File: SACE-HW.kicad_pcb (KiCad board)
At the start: 2 copper layers, 100 x 100 mm, 189 parts, among them IC201 1769205241, J201 Header_Male_Pin_2.54mm_1X2_,_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, J202 1935161, J203 2350514-8, J301 Header_Male_Pin_2.54mm_1X6_,_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, J302 XH-4A connector, J401 1935161, J402 1935161, J403 RF1-01K-D-00-50-BK-HDW, J404 RF1-01K-D-00-50-BK-HDW, J501 Header_Male_Pin_2.54mm_1X4_,_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, J502 690-005-299-043, J601 XH-4A connector, J602 XH-4A connector, J603 2350514-8, J604 2350514-8, J605 2350514-8, J701 2350514-8, J801 MEM2075-00-140-01-A, J901 2350514-8, J902 2350514-8, Q401 MCB90N12A-TP, Q901 PMV20XNER, Q902 PMV20XNER, Q903 PMV20XNER, Q904 PMV20XNER, Q905 PMV20XNER, Q906 PMV20XNER, Q907 PMV20XNER, Q908 PMV20XNER, SW301 PTS645SM43SMTR92, SW302 PTS645SM43SMTR92, U201 AZ1117IH-3.3TRG1, U202 OKI-78SR-5_1.5-W36H-C, U203 AZ1117IH-3.3TRG1, U301 STM32F446RE, U401 LTV-816S, U402 TMCS1101A3UQDT, U403 MCP6L04T-E/SL, U501 MCP2221A-I_SL, U601 MCP4728T-E_UN, U602 TLA2528IRTER, U603 TLV9302IDR, U604 TLA2528IRTER, U701 74LVC4245APW_118

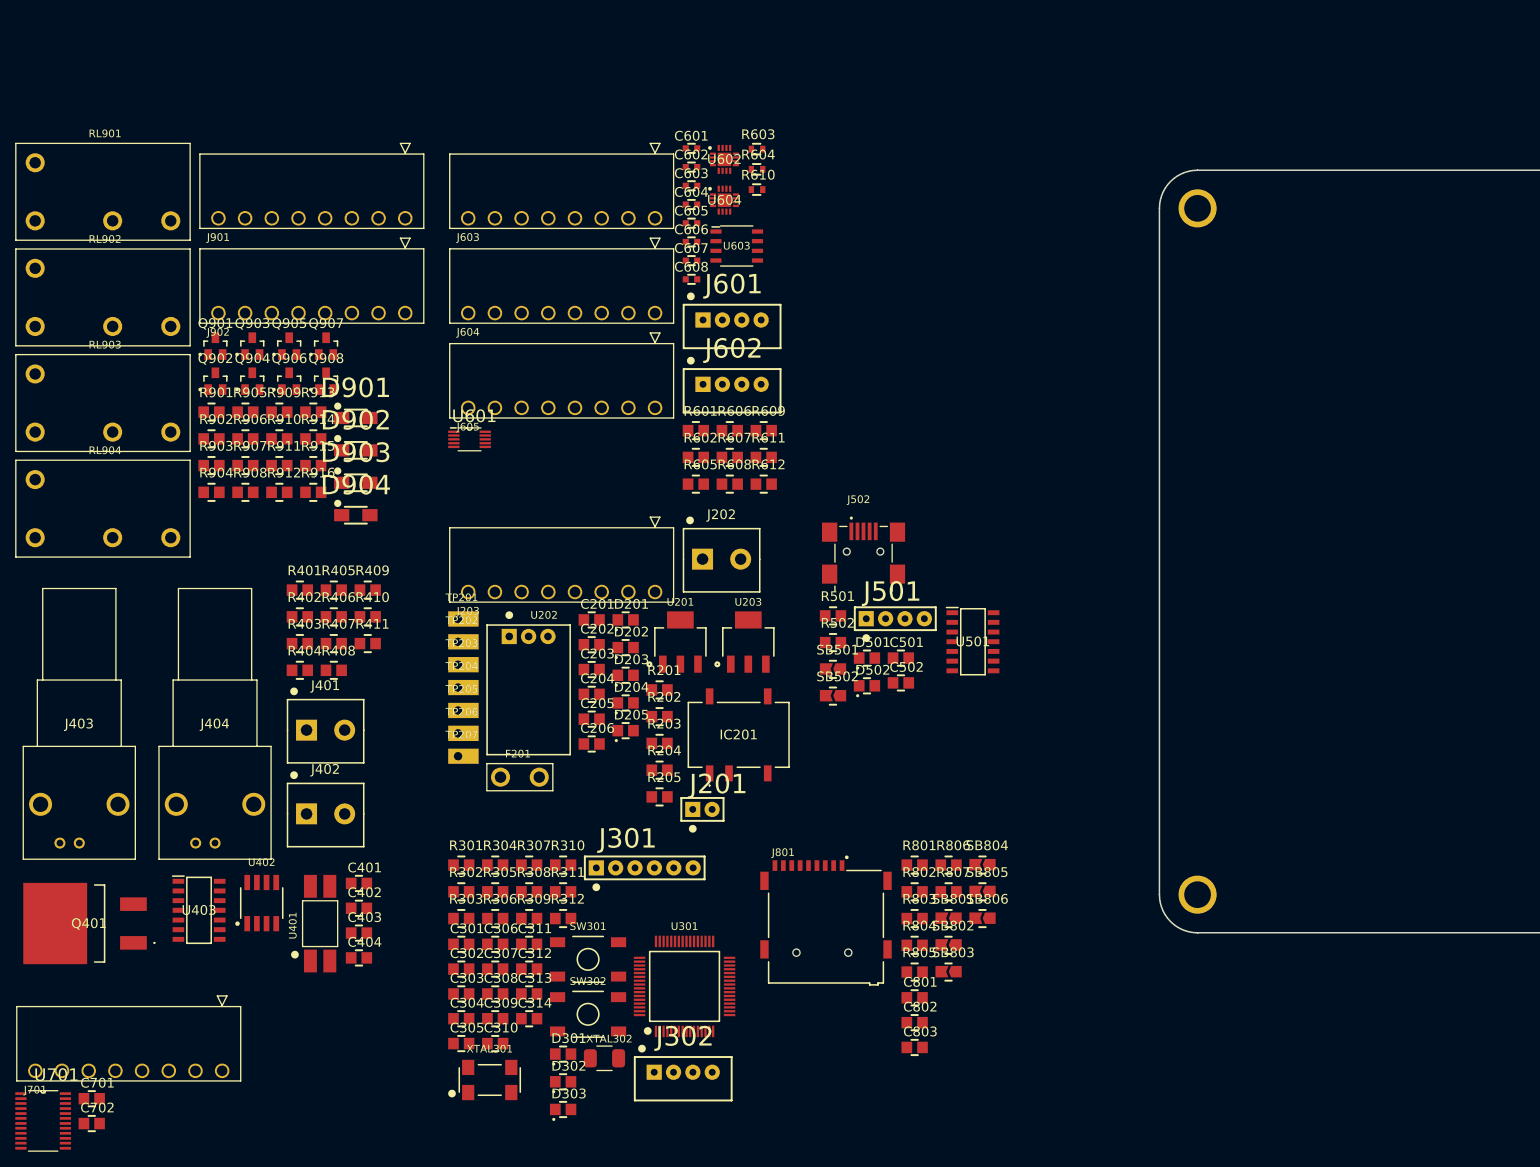
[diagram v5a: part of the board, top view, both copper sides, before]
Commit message: update schematic
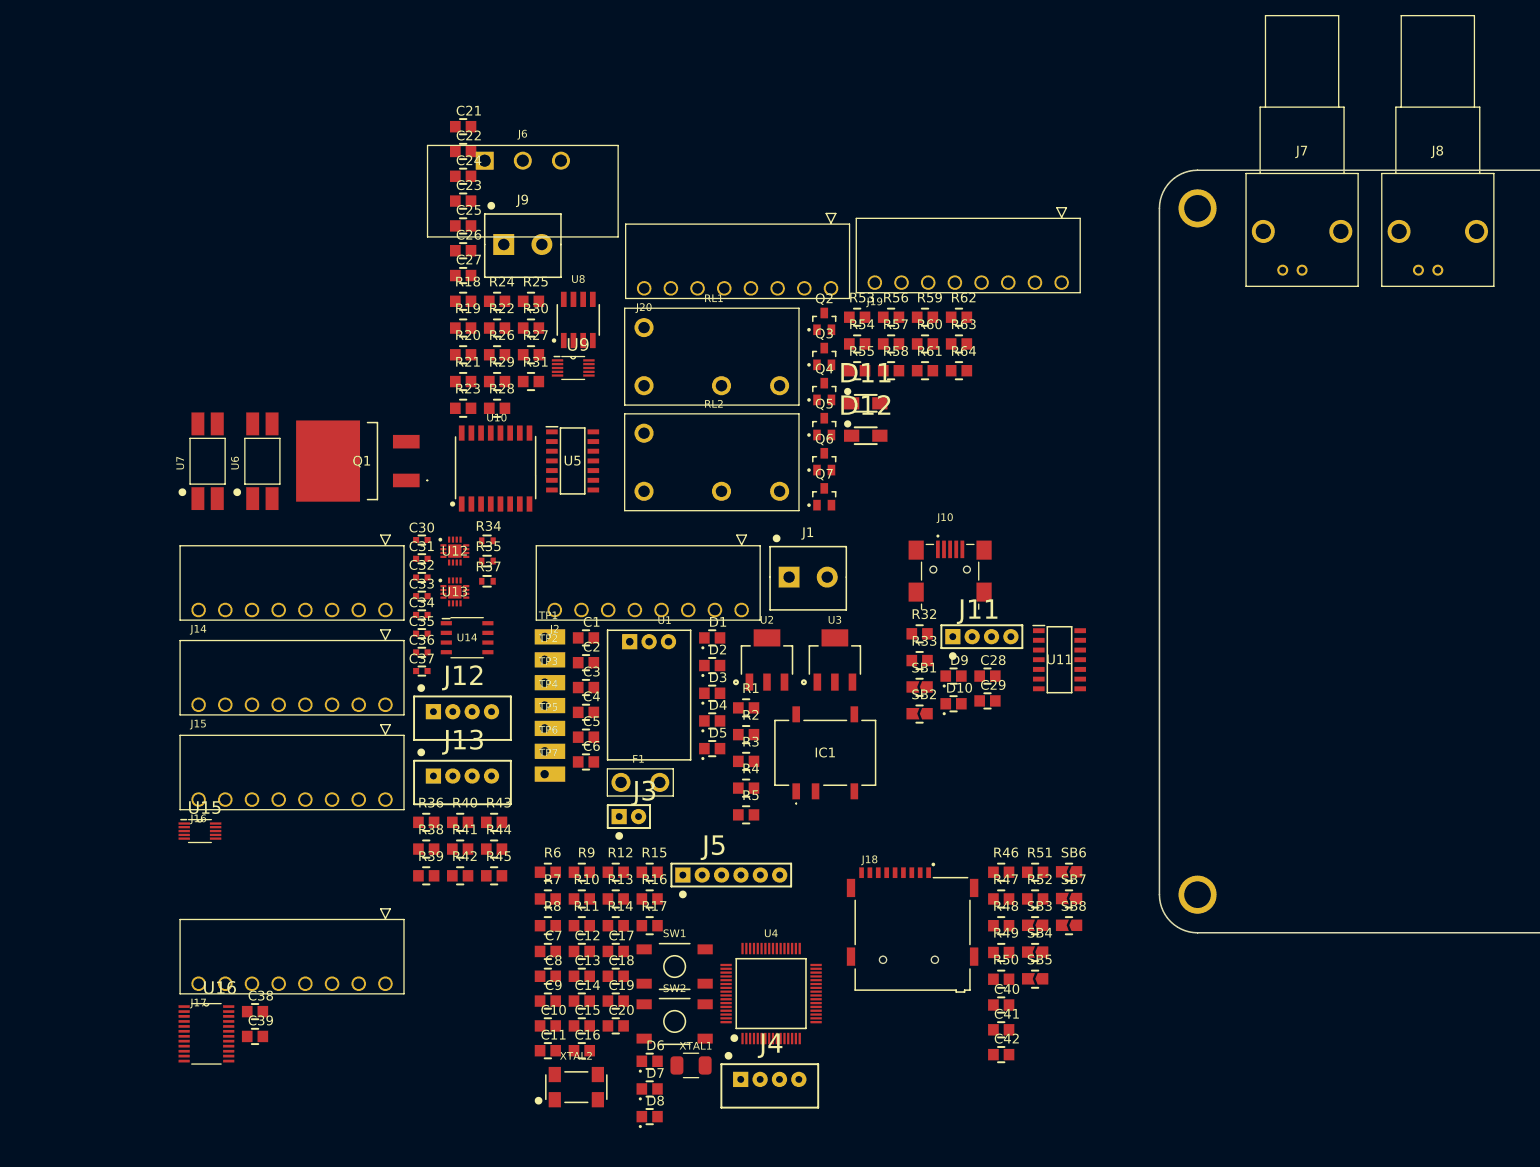
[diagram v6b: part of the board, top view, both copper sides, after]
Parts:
- removed C201, C203: 885012107005, Capacitors:C0805
- removed C202, C206: 885012107014, Capacitors:C0805
- removed C204, C205, C312: 885012107018, Capacitors:C0805
- removed C301, C307, C310, C311, C313, C314, C401, C403, C501, C502, C701, C702, C802, C803: 885012207098, Capacitors:C0805
- removed C302, C303: 885012007027, Capacitors:C0805
- removed C304, C308, C801: 885012107015, Capacitors:C0805
- removed C305, C306: 885012007053, Capacitors:C0805
- removed C309: 885012207092, Capacitors:C0805
- removed C402, C404: 885012207103, Capacitors:C0805
- removed C601, C602, C603, C604, C605, C606, C607, C608: 885012107015, Capacitors:C0603
- removed D201, D202, D203, D204, D205, D301, D501: 150080VS75000, Diodes:LED_0805_GREEN
- removed D302, D502: 150080YS75000, Diodes:LED_0805_YELLOW
- removed D303: 150080RS75000, Diodes:LED_0805_RED
- removed D901, D902, D903, D904: DSS16U, Diodes:SOD-123FL
- removed F201: 39511000440, Fuses:TE5_395
- removed IC201: 1769205241, IC:1769205241
- removed J201: Header_Male_Pin_2.54mm_1X2_,_Unshrouded, Connectors:Headers_2.54mm_1X2
- removed J202, J401, J402: 1935161, Connectors:1935161
- removed J203, J603, J604, J605, J701, J901, J902: 2350514-8, Connectors:CONN8_2350514-8_TEC
- removed J301: Header_Male_Pin_2.54mm_1X6_,_Unshrouded, Connectors:Headers_2.54mm_1X6
- removed J302, J601, J602: XH-4A connector, Connectors:XH-4A
- removed J403, J404: RF1-01K-D-00-50-BK-HDW, Connectors:RF101KD0050
- removed J501: Header_Male_Pin_2.54mm_1X4_,_Unshrouded, Connectors:Headers_2.54mm_1X4
- removed J502: 690-005-299-043, Connectors:EDAC_690-005-299-043
- removed J801: MEM2075-00-140-01-A, Connectors:GCT_MEM2075-00-140-01-A
- removed Q401: MCB90N12A-TP, IC:MCB90N12ATP
- removed Q901, Q902, Q903, Q904, Q905, Q906, Q907, Q908: PMV20XNER, IC:SOT-23-3
- removed R201, R204, R403, R405, R406, R408, R410: RC0805FR-075K6L, Resistors:R0805
- removed R202, R205, R310, R311, R312, R402, R501, R502, R605, R609: RC0805JR-072K2L, Resistors:R0805
- removed R203: RC0805JR-0733KL, Resistors:R0805
- removed R301, R606, R607, R611, R612, R905, R906, R907, R908, R913, R914, R915, R916: RC0805JR-0710KL, Resistors:R0805
- removed R302, R303: RC0805JR-070RL, Resistors:R0805
- removed R304, R305, R601, R602: RC0805JR-074K7L, Resistors:R0805
- removed R306, R307, R802: RC0805JR-07150RL, Resistors:R0805
- removed R308, R309: RC0805JR-07470RL, Resistors:R0805
- removed R401, R901, R902, R903, R904, R909, R910, R911, R912: RC0805JR-07330RL, Resistors:R0805
- removed R404, R409: RMCF0805FT10M0, Resistors:R0805
- removed R407, R411: RC0805FR-07200KL, Resistors:R0805
- removed R603, R604, R610: RC0805JR-070RL, Resistors:R0603
- removed R608: RC0805JR-07100KL, Resistors:R0805
- removed R801, R803, R804, R805, R806, R807: RC0805FR-0747KL, Resistors:R0805
- removed RL901, RL902, RL903, RL904: ALQ312, Relays:ALQ312
- removed SB501, SB502, SB801, SB802, SB803, SB804, SB805, SB806: Solder_Bridge, Connectors:Solder_bridge_0805
- removed SW301, SW302: PTS645SM43SMTR92, Switches:PTS645_6X6X4_SMD
- removed TP201, TP202, TP203, TP204, TP205, TP206, TP207: Test_Point_THM, Connectors:Keystone_5001
- removed U201, U203: AZ1117IH-3.3TRG1, IC:SOT-223-3
- removed U202: OKI-78SR-5_1.5-W36H-C, Assembly:OKI-78SR_Horizontal
- removed U301: STM32F446RE, IC:LQFP-64
- removed U401: LTV-816S, IC:4-SMD
- removed U402: TMCS1101A3UQDT, IC:SOIC-8
- removed U403: MCP6L04T-E/SL, IC:SOIC127P600X175-14N
- removed U501: MCP2221A-I_SL, IC:SOIC127P600X175-14N
- removed U601: MCP4728T-E_UN, IC:SOP50P490X110-10N
- removed U602, U604: TLA2528IRTER, IC:QFN50P300X300X80-17N-D
- removed U603: TLV9302IDR, Assembly:IC8_TLV9302IDR_TEX
- removed U701: 74LVC4245APW_118, IC:SOP65P640X110-24N
- removed XTAL301: ABS25-32.768KHZ-6-T, Crystals:ABS25
- removed XTAL302: 7A-8.000MAHJ-T, Crystals:TXC_7A_Series
- added C1: 885012107018, Capacitors:C0805, F.Cu at (94.3, 85.1)
- added C10: 885012007027, Capacitors:C0805, F.Cu at (89.3, 136.0)
- added C11: 885012107015, Capacitors:C0805, F.Cu at (89.3, 139.3)
- added C12: 885012207092, Capacitors:C0805, F.Cu at (93.7, 126.2)
- added C13: 885012007027, Capacitors:C0805, F.Cu at (93.7, 129.5)
- added C14: 885012107015, Capacitors:C0805, F.Cu at (93.7, 132.8)
- added C15: 885012207098, Capacitors:C0805, F.Cu at (93.7, 136.0)
- added C16: 885012207098, Capacitors:C0805, F.Cu at (93.7, 139.3)
- added C17: 885012107018, Capacitors:C0805, F.Cu at (98.2, 126.2)
- added C18: 885012207098, Capacitors:C0805, F.Cu at (98.2, 129.5)
- added C19: 885012207098, Capacitors:C0805, F.Cu at (98.2, 132.8)
- added C2: 885012107018, Capacitors:C0805, F.Cu at (94.3, 88.4)
- added C20: 885012207098, Capacitors:C0805, F.Cu at (98.2, 136.0)
- added C21: 885012207103, Capacitors:C0805, F.Cu at (78.2, 18.1)
- added C22: 885012207098, Capacitors:C0805, F.Cu at (78.2, 21.3)
- added C23: 885012207098, Capacitors:C0805, F.Cu at (78.2, 27.8)
- added C24: 885012207103, Capacitors:C0805, F.Cu at (78.2, 24.6)
- added C25: 885012207103, Capacitors:C0805, F.Cu at (78.2, 31.1)
- added C26: 885012207098, Capacitors:C0805, F.Cu at (78.2, 34.4)
- added C27: 885012207103, Capacitors:C0805, F.Cu at (78.2, 37.6)
- added C28: 885012207098, Capacitors:C0805, F.Cu at (146.9, 90.1)
- added C29: 885012207098, Capacitors:C0805, F.Cu at (146.9, 93.4)
- added C3: 885012107014, Capacitors:C0805, F.Cu at (94.3, 91.6)
- added C30: 885012107015, Capacitors:C0603, F.Cu at (73.0, 72.3)
- added C31: 885012107015, Capacitors:C0603, F.Cu at (73.0, 74.8)
- added C32: 885012107015, Capacitors:C0603, F.Cu at (73.0, 77.2)
- added C33: 885012107015, Capacitors:C0603, F.Cu at (73.0, 79.7)
- added C34: 885012107015, Capacitors:C0603, F.Cu at (73.0, 82.1)
- added C35: 885012107015, Capacitors:C0603, F.Cu at (73.0, 84.6)
- added C36: 885012107015, Capacitors:C0603, F.Cu at (73.0, 87.0)
- added C37: 885012107015, Capacitors:C0603, F.Cu at (73.0, 89.5)
- added C38: 885012207098, Capacitors:C0805, F.Cu at (50.9, 134.1)
- added C39: 885012207098, Capacitors:C0805, F.Cu at (50.9, 137.4)
- added C4: 885012107014, Capacitors:C0805, F.Cu at (94.3, 94.9)
- added C40: 885012207098, Capacitors:C0805, F.Cu at (148.7, 133.3)
- added C41: 885012107015, Capacitors:C0805, F.Cu at (148.7, 136.5)
- added C42: 885012207098, Capacitors:C0805, F.Cu at (148.7, 139.8)
- added C5: 885012107005, Capacitors:C0805, F.Cu at (94.3, 98.1)
- added C6: 885012107005, Capacitors:C0805, F.Cu at (94.3, 101.4)
- added C7: 885012007053, Capacitors:C0805, F.Cu at (89.3, 126.2)
- added C8: 885012207098, Capacitors:C0805, F.Cu at (89.3, 129.5)
- added C9: 885012007053, Capacitors:C0805, F.Cu at (89.3, 132.8)
- added D1: 150080VS75000, Diodes:LED_0805_GREEN, F.Cu at (110.8, 85.1)
- added D10: 150080YS75000, Diodes:LED_0805_YELLOW, F.Cu at (142.5, 93.8)
- added D11: DSS16U, Diodes:SOD-123FL, F.Cu at (132.0, 54.4)
- added D12: DSS16U, Diodes:SOD-123FL, F.Cu at (132.0, 58.6)
- added D2: 150080VS75000, Diodes:LED_0805_GREEN, F.Cu at (110.8, 88.8)
- added D3: 150080VS75000, Diodes:LED_0805_GREEN, F.Cu at (110.8, 92.4)
- added D4: 150080VS75000, Diodes:LED_0805_GREEN, F.Cu at (110.8, 96.0)
- added D5: 150080VS75000, Diodes:LED_0805_GREEN, F.Cu at (110.8, 99.6)
- added D6: 150080VS75000, Diodes:LED_0805_GREEN, F.Cu at (102.6, 140.6)
- added D7: 150080YS75000, Diodes:LED_0805_YELLOW, F.Cu at (102.6, 144.3)
- added D8: 150080RS75000, Diodes:LED_0805_RED, F.Cu at (102.6, 147.9)
- added D9: 150080VS75000, Diodes:LED_0805_GREEN, F.Cu at (142.5, 90.1)
- added F1: 39511000440, Fuses:TE5_395, F.Cu at (102.4, 104.1)
- added IC1: 1769205241, IC:1769205241, F.Cu at (126.7, 100.2)
- added J1: 1935161, Connectors:1935161, F.Cu at (124.4, 77.2)
- added J10: 690-005-299-043, Connectors:EDAC_690-005-299-043, F.Cu at (143.1, 76.2)
- added J11: Header_Male_Pin_2.54mm_1X4_,_Unshrouded, Connectors:Headers_2.54mm_1X4, F.Cu at (143.4, 85.0)
- added J12: XH-4A connector, Connectors:XH-4A, F.Cu at (75.3, 94.8)
- added J13: XH-4A connector, Connectors:XH-4A, F.Cu at (75.3, 103.2)
- added J14: 2350514-8, Connectors:CONN8_2350514-8_TEC, F.Cu at (69.0, 81.5)
- added J15: 2350514-8, Connectors:CONN8_2350514-8_TEC, F.Cu at (69.0, 93.9)
- added J16: 2350514-8, Connectors:CONN8_2350514-8_TEC, F.Cu at (69.0, 106.3)
- added J17: 2350514-8, Connectors:CONN8_2350514-8_TEC, F.Cu at (69.0, 130.5)
- added J18: MEM2075-00-140-01-A, Connectors:GCT_MEM2075-00-140-01-A, F.Cu at (137.7, 127.3)
- added J19: 2350514-8, Connectors:CONN8_2350514-8_TEC, F.Cu at (157.7, 38.5)
- added J2: 2350514-8, Connectors:CONN8_2350514-8_TEC, F.Cu at (115.7, 81.5)
- added J20: 2350514-8, Connectors:CONN8_2350514-8_TEC, F.Cu at (127.4, 39.3)
- added J3: Header_Male_Pin_2.54mm_1X2_,_Unshrouded, Connectors:Headers_2.54mm_1X2, F.Cu at (99.7, 108.6)
- added J4: XH-4A connector, Connectors:XH-4A, F.Cu at (115.6, 143.0)
- added J5: Header_Male_Pin_2.54mm_1X6_,_Unshrouded, Connectors:Headers_2.54mm_1X6, F.Cu at (108.0, 116.2)
- added J6: 691317710003, Connectors:691317710003, F.Cu at (87.0, 22.5)
- added J7: RF1-01K-D-00-50-BK-HDW, Connectors:RF101KD0050, F.Cu at (189.2, 36.9)
- added J8: RF1-01K-D-00-50-BK-HDW, Connectors:RF101KD0050, F.Cu at (207.0, 36.9)
- added J9: 1935161, Connectors:1935161, F.Cu at (87.0, 33.5)
- added Q1: MCB90N12A-TP, IC:MCB90N12ATP, F.Cu at (63.5, 61.9)
- added Q2: PMV20XNER, IC:SOT-23-3, F.Cu at (126.5, 43.6)
- added Q3: PMV20XNER, IC:SOT-23-3, F.Cu at (126.5, 48.2)
- added Q4: PMV20XNER, IC:SOT-23-3, F.Cu at (126.5, 52.8)
- added Q5: PMV20XNER, IC:SOT-23-3, F.Cu at (126.5, 57.4)
- added Q6: PMV20XNER, IC:SOT-23-3, F.Cu at (126.5, 62.0)
- added Q7: PMV20XNER, IC:SOT-23-3, F.Cu at (126.5, 66.6)
- added R1: RC0805JR-0733KL, Resistors:R0805, F.Cu at (115.3, 94.3)
- added R10: RC0805JR-07470RL, Resistors:R0805, F.Cu at (93.7, 119.4)
- added R11: RC0805JR-070RL, Resistors:R0805, F.Cu at (93.7, 122.9)
- added R12: RC0805JR-072K2L, Resistors:R0805, F.Cu at (98.2, 115.9)
- added R13: RC0805JR-072K2L, Resistors:R0805, F.Cu at (98.2, 119.4)
- added R14: RC0805JR-0710KL, Resistors:R0805, F.Cu at (98.2, 122.9)
- added R15: RC0805JR-072K2L, Resistors:R0805, F.Cu at (102.6, 115.9)
- added R16: RC0805JR-07150RL, Resistors:R0805, F.Cu at (102.6, 119.4)
- added R17: RC0805JR-074K7L, Resistors:R0805, F.Cu at (102.6, 122.9)
- added R18: RMCF0805FT10M0, Resistors:R0805, F.Cu at (78.2, 41.0)
- added R19: RC0805FR-07200KL, Resistors:R0805, F.Cu at (78.2, 44.5)
- added R2: RC0805FR-075K6L, Resistors:R0805, F.Cu at (115.3, 97.8)
- added R20: RMCF0805FT10M0, Resistors:R0805, F.Cu at (78.2, 48.0)
- added R21: RC0805FR-07200KL, Resistors:R0805, F.Cu at (78.2, 51.5)
- added R22: RC0805JR-072K2L, Resistors:R0805, F.Cu at (82.6, 44.5)
- added R23: RC0805FR-075K6L, Resistors:R0805, F.Cu at (78.2, 55.0)
- added R24: RC0805FR-075K6L, Resistors:R0805, F.Cu at (82.6, 41.0)
- added R25: RC0805FR-075K6L, Resistors:R0805, F.Cu at (87.1, 41.0)
- added R26: RC0805FR-075K6L, Resistors:R0805, F.Cu at (82.6, 48.0)
- added R27: RC0805JR-07330RL, Resistors:R0805, F.Cu at (87.1, 48.0)
- added R28: RC0805FR-075K6L, Resistors:R0805, F.Cu at (82.6, 55.0)
- added R29: RC0805JR-072K2L, Resistors:R0805, F.Cu at (82.6, 51.5)
- added R3: RC0805FR-075K6L, Resistors:R0805, F.Cu at (115.3, 101.3)
- added R30: RC0805FR-075K6L, Resistors:R0805, F.Cu at (87.1, 44.5)
- added R31: RC0805JR-0710KL, Resistors:R0805, F.Cu at (87.1, 51.5)
- added R32: RC0805JR-072K2L, Resistors:R0805, F.Cu at (138.0, 84.6)
- added R33: RC0805JR-072K2L, Resistors:R0805, F.Cu at (138.0, 88.1)
- added R34: RC0805JR-070RL, Resistors:R0603, F.Cu at (81.6, 72.4)
- added R35: RC0805JR-070RL, Resistors:R0603, F.Cu at (81.6, 75.1)
- added R36: RC0805JR-070RL, Resistors:R0805, F.Cu at (73.3, 109.3)
- added R37: RC0805JR-070RL, Resistors:R0603, F.Cu at (81.6, 77.7)
- added R38: RC0805JR-074K7L, Resistors:R0805, F.Cu at (73.3, 112.8)
- added R39: RC0805JR-074K7L, Resistors:R0805, F.Cu at (73.3, 116.3)
- added R4: RC0805JR-072K2L, Resistors:R0805, F.Cu at (115.3, 104.8)
- added R40: RC0805JR-0710KL, Resistors:R0805, F.Cu at (77.8, 109.3)
- added R41: RC0805JR-0710KL, Resistors:R0805, F.Cu at (77.8, 112.8)
- added R42: RC0805JR-0710KL, Resistors:R0805, F.Cu at (77.8, 116.3)
- added R43: RC0805JR-0710KL, Resistors:R0805, F.Cu at (82.2, 109.3)
- added R44: RC0805JR-072K2L, Resistors:R0805, F.Cu at (82.2, 112.8)
- added R45: RC0805JR-072K2L, Resistors:R0805, F.Cu at (82.2, 116.3)
- added R46: RC0805FR-0747KL, Resistors:R0805, F.Cu at (148.7, 115.9)
- added R47: RC0805FR-0747KL, Resistors:R0805, F.Cu at (148.7, 119.4)
- added R48: RC0805FR-0747KL, Resistors:R0805, F.Cu at (148.7, 122.9)
- added R49: RC0805FR-0747KL, Resistors:R0805, F.Cu at (148.7, 126.4)
- added R5: RC0805JR-072K2L, Resistors:R0805, F.Cu at (115.3, 108.3)
- added R50: RC0805FR-0747KL, Resistors:R0805, F.Cu at (148.7, 129.9)
- added R51: RC0805JR-07150RL, Resistors:R0805, F.Cu at (153.2, 115.9)
- added R52: RC0805FR-0747KL, Resistors:R0805, F.Cu at (153.2, 119.4)
- added R53: RC0805JR-0710KL, Resistors:R0805, F.Cu at (129.8, 43.1)
- added R54: RC0805JR-07330RL, Resistors:R0805, F.Cu at (129.8, 46.6)
- added R55: RC0805JR-0710KL, Resistors:R0805, F.Cu at (129.8, 50.1)
- added R56: RC0805JR-0710KL, Resistors:R0805, F.Cu at (134.3, 43.1)
- added R57: RC0805JR-07330RL, Resistors:R0805, F.Cu at (134.3, 46.6)
- added R58: RC0805JR-07330RL, Resistors:R0805, F.Cu at (134.3, 50.1)
- added R59: RC0805JR-0710KL, Resistors:R0805, F.Cu at (138.7, 43.1)
- added R6: RC0805JR-074K7L, Resistors:R0805, F.Cu at (89.3, 115.9)
- added R60: RC0805JR-0710KL, Resistors:R0805, F.Cu at (138.7, 46.6)
- added R61: RC0805JR-07330RL, Resistors:R0805, F.Cu at (138.7, 50.1)
- added R62: RC0805JR-07330RL, Resistors:R0805, F.Cu at (143.2, 43.1)
- added R63: RC0805JR-0710KL, Resistors:R0805, F.Cu at (143.2, 46.6)
- added R64: RC0805JR-07330RL, Resistors:R0805, F.Cu at (143.2, 50.1)
- added R7: RC0805JR-070RL, Resistors:R0805, F.Cu at (89.3, 119.4)
- added R8: RC0805JR-07150RL, Resistors:R0805, F.Cu at (89.3, 122.9)
- added R9: RC0805JR-07470RL, Resistors:R0805, F.Cu at (93.7, 115.9)
- added RL1: ALQ312, Relays:ALQ312, F.Cu at (111.8, 48.2)
- added RL2: ALQ312, Relays:ALQ312, F.Cu at (111.8, 62.1)
- added SB1: Solder_Bridge, Connectors:Solder_bridge_0805, F.Cu at (139.1, 91.6)
- added SB2: Solder_Bridge, Connectors:Solder_bridge_0805, F.Cu at (139.1, 95.1)
- added SB3: Solder_Bridge, Connectors:Solder_bridge_0805, F.Cu at (154.2, 122.8)
- added SB4: Solder_Bridge, Connectors:Solder_bridge_0805, F.Cu at (154.2, 126.3)
- added SB5: Solder_Bridge, Connectors:Solder_bridge_0805, F.Cu at (154.2, 129.8)
- added SB6: Solder_Bridge, Connectors:Solder_bridge_0805, F.Cu at (158.7, 115.8)
- added SB7: Solder_Bridge, Connectors:Solder_bridge_0805, F.Cu at (158.7, 119.3)
- added SB8: Solder_Bridge, Connectors:Solder_bridge_0805, F.Cu at (158.7, 122.8)
- added SW1: PTS645SM43SMTR92, Switches:PTS645_6X6X4_SMD, F.Cu at (106.9, 128.2)
- added SW2: PTS645SM43SMTR92, Switches:PTS645_6X6X4_SMD, F.Cu at (106.9, 135.4)
- added TP1: Test_Point_THM, Connectors:Keystone_5001, F.Cu at (89.9, 85.0)
- added TP2: Test_Point_THM, Connectors:Keystone_5001, F.Cu at (89.9, 88.0)
- added TP3: Test_Point_THM, Connectors:Keystone_5001, F.Cu at (89.9, 91.0)
- added TP4: Test_Point_THM, Connectors:Keystone_5001, F.Cu at (89.9, 94.0)
- added TP5: Test_Point_THM, Connectors:Keystone_5001, F.Cu at (89.9, 97.0)
- added TP6: Test_Point_THM, Connectors:Keystone_5001, F.Cu at (89.9, 100.0)
- added TP7: Test_Point_THM, Connectors:Keystone_5001, F.Cu at (89.9, 103.0)
- added U1: OKI-78SR-5_1.5-W36H-C, Assembly:OKI-78SR_Horizontal, F.Cu at (103.6, 85.6)
- added U10: ISO7341CQDWQ1, IC:SOIC-16-wide, F.Cu at (83.4, 59.4)
- added U11: MCP2221A-I_SL, IC:SOIC127P600X175-14N, F.Cu at (157.4, 88.0)
- added U12: TLA2528IRTER, IC:QFN50P300X300X80-17N-D, F.Cu at (78.1, 73.7)
- added U13: TLA2528IRTER, IC:QFN50P300X300X80-17N-D, F.Cu at (78.1, 79.1)
- added U14: TLV9302IDR, Assembly:IC8_TLV9302IDR_TEX, F.Cu at (79.7, 85.1)
- added U15: MCP4728T-E_UN, IC:SOP50P490X110-10N, F.Cu at (44.7, 110.5)
- added U16: 74LVC4245APW_118, IC:SOP65P640X110-24N, F.Cu at (45.5, 137.0)
- added U2: AZ1117IH-3.3TRG1, IC:SOT-223-3, F.Cu at (119.0, 88.0)
- added U3: AZ1117IH-3.3TRG1, IC:SOT-223-3, F.Cu at (127.9, 88.0)
- added U4: STM32F446RE, IC:LQFP-64, F.Cu at (119.6, 131.8)
- added U5: MCP6L04T-E/SL, IC:SOIC127P600X175-14N, F.Cu at (93.5, 61.9)
- added U6: LTV-816S, IC:4-SMD, F.Cu at (52.9, 62.0)
- added U7: LTV-816S, IC:4-SMD, F.Cu at (45.7, 62.0)
- added U8: TMCS1101A3UQDT, IC:SOIC-8, F.Cu at (94.3, 43.4)
- added U9: ADC124S021CIMM, IC:SOP50P490X110-10N, F.Cu at (93.6, 49.7)
- added XTAL1: 7A-8.000MAHJ-T, Crystals:TXC_7A_Series, F.Cu at (109.1, 141.2)
- added XTAL2: ABS25-32.768KHZ-6-T, Crystals:ABS25, F.Cu at (94.0, 144.0)
- renumbered H101 to H1, H102 to H2, H103 to H3, H104 to H4

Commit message: update
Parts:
- removed C1, C17, C2: 885012107018, Capacitors:C0805
- removed C10, C13: 885012007027, Capacitors:C0805
- removed C11, C14, C41: 885012107015, Capacitors:C0805
- removed C12: 885012207092, Capacitors:C0805
- removed C15, C16, C18, C19, C20, C22, C23, C26, C28, C29, C38, C39, C40, C42, C8: 885012207098, Capacitors:C0805
- removed C21, C24, C25, C27: 885012207103, Capacitors:C0805
- removed C3, C4: 885012107014, Capacitors:C0805
- removed C30, C31, C32, C33, C34, C35, C36, C37: 885012107015, Capacitors:C0603
- removed C5, C6: 885012107005, Capacitors:C0805
- removed C7, C9: 885012007053, Capacitors:C0805
- removed D1, D2, D3, D4, D5, D6, D9: 150080VS75000, Diodes:LED_0805_GREEN
- removed D10, D7: 150080YS75000, Diodes:LED_0805_YELLOW
- removed D11, D12: DSS16U, Diodes:SOD-123FL
- removed D8: 150080RS75000, Diodes:LED_0805_RED
- removed F1: 39511000440, Fuses:TE5_395
- removed H1, H2, H3, H4: Mounting-Hole-M3, Connectors:Mounting_Hole_3mm
- removed IC1: 1769205241, IC:1769205241
- removed J1, J9: 1935161, Connectors:1935161
- removed J10: 690-005-299-043, Connectors:EDAC_690-005-299-043
- removed J11: Header_Male_Pin_2.54mm_1X4_,_Unshrouded, Connectors:Headers_2.54mm_1X4
- removed J12, J13, J4: XH-4A connector, Connectors:XH-4A
- removed J14, J15, J16, J17, J19, J2, J20: 2350514-8, Connectors:CONN8_2350514-8_TEC
- removed J18: MEM2075-00-140-01-A, Connectors:GCT_MEM2075-00-140-01-A
- removed J3: Header_Male_Pin_2.54mm_1X2_,_Unshrouded, Connectors:Headers_2.54mm_1X2
- removed J5: Header_Male_Pin_2.54mm_1X6_,_Unshrouded, Connectors:Headers_2.54mm_1X6
- removed J6: 691317710003, Connectors:691317710003
- removed J7, J8: RF1-01K-D-00-50-BK-HDW, Connectors:RF101KD0050
- removed Q1: MCB90N12A-TP, IC:MCB90N12ATP
- removed Q2, Q3, Q4, Q5, Q6, Q7: PMV20XNER, IC:SOT-23-3
- removed R1: RC0805JR-0733KL, Resistors:R0805
- removed R10, R9: RC0805JR-07470RL, Resistors:R0805
- removed R11, R36, R7: RC0805JR-070RL, Resistors:R0805
- removed R12, R13, R15, R22, R29, R32, R33, R4, R44, R45, R5: RC0805JR-072K2L, Resistors:R0805
- removed R14, R31, R40, R41, R42, R43, R53, R55, R56, R59, R60, R63: RC0805JR-0710KL, Resistors:R0805
- removed R16, R51, R8: RC0805JR-07150RL, Resistors:R0805
- removed R17, R38, R39, R6: RC0805JR-074K7L, Resistors:R0805
- removed R18, R20: RMCF0805FT10M0, Resistors:R0805
- removed R19, R21: RC0805FR-07200KL, Resistors:R0805
- removed R2, R23, R24, R25, R26, R28, R3, R30: RC0805FR-075K6L, Resistors:R0805
- removed R27, R54, R57, R58, R61, R62, R64: RC0805JR-07330RL, Resistors:R0805
- removed R34, R35, R37: RC0805JR-070RL, Resistors:R0603
- removed R46, R47, R48, R49, R50, R52: RC0805FR-0747KL, Resistors:R0805
- removed RL1, RL2: ALQ312, Relays:ALQ312
- removed SB1, SB2, SB3, SB4, SB5, SB6, SB7, SB8: Solder_Bridge, Connectors:Solder_bridge_0805
- removed SW1, SW2: PTS645SM43SMTR92, Switches:PTS645_6X6X4_SMD
- removed TP1, TP2, TP3, TP4, TP5, TP6, TP7: Test_Point_THM, Connectors:Keystone_5001
- removed U1: OKI-78SR-5_1.5-W36H-C, Assembly:OKI-78SR_Horizontal
- removed U10: ISO7341CQDWQ1, IC:SOIC-16-wide
- removed U11: MCP2221A-I_SL, IC:SOIC127P600X175-14N
- removed U12, U13: TLA2528IRTER, IC:QFN50P300X300X80-17N-D
- removed U14: TLV9302IDR, Assembly:IC8_TLV9302IDR_TEX
- removed U15: MCP4728T-E_UN, IC:SOP50P490X110-10N
- removed U16: 74LVC4245APW_118, IC:SOP65P640X110-24N
- removed U2, U3: AZ1117IH-3.3TRG1, IC:SOT-223-3
- removed U4: STM32F446RE, IC:LQFP-64
- removed U5: MCP6L04T-E/SL, IC:SOIC127P600X175-14N
- removed U6, U7: LTV-816S, IC:4-SMD
- removed U8: TMCS1101A3UQDT, IC:SOIC-8
- removed U9: ADC124S021CIMM, IC:SOP50P490X110-10N
- removed XTAL1: 7A-8.000MAHJ-T, Crystals:TXC_7A_Series
- removed XTAL2: ABS25-32.768KHZ-6-T, Crystals:ABS25
- added C201: 885012107005, Capacitors:C0805, F.Cu at (110.4, 86.1)
- added C202: 885012107014, Capacitors:C0805, F.Cu at (103.2, 93.5)
- added C203: 885012107005, Capacitors:C0805, F.Cu at (129.2, 130.5)
- added C204: 885012107018, Capacitors:C0805, F.Cu at (145.5, 54.8)
- added C205: 885012107018, Capacitors:C0805, F.Cu at (154.8, 54.8)
- added C206: 885012107014, Capacitors:C0805, F.Cu at (121.2, 123.4)
- added C301: 885012207098, Capacitors:C0805, F.Cu at (146.8, 150.5)
- added C401: 885012207098, Capacitors:C0805, F.Cu at (166.1, -28.8)
- added C402: 885012207103, Capacitors:C0805, F.Cu at (166.1, -25.6)
- added C403: 885012207098, Capacitors:C0805, F.Cu at (166.1, -22.3)
- added C404: 885012207103, Capacitors:C0805, F.Cu at (166.1, -19.0)
- added C405: 885012207098, Capacitors:C0805, F.Cu at (166.1, -15.8)
- added C406: 885012207103, Capacitors:C0805, F.Cu at (166.1, -12.5)
- added C501: 885012107015, Capacitors:C0805, F.Cu at (87.9, 119.4)
- added C502: 885012107015, Capacitors:C0805, F.Cu at (87.9, 117.0)
- added C503: 885012107015, Capacitors:C0805, F.Cu at (153.2, 88.2)
- added C504: 885012107015, Capacitors:C0805, F.Cu at (150.8, 88.2)
- added C505: 885012107015, Capacitors:C0805, F.Cu at (101.4, 109.8)
- added C506: 885012107015, Capacitors:C0805, F.Cu at (148.4, 91.2)
- added C507: 885012107015, Capacitors:C0805, F.Cu at (101.4, 118.8)
- added C601: 885012207098, Capacitors:C0805, F.Cu at (153.4, 180.9)
- added C602: 885012207098, Capacitors:C0805, F.Cu at (147.6, 180.9)
- added C701: 885012107015, Capacitors:C0805, F.Cu at (105.4, 169.7)
- added C702: 885012207098, Capacitors:C0805, F.Cu at (103.3, 167.4)
- added C703: 885012207098, Capacitors:C0805, F.Cu at (96.0, 167.7)
- added D201: 150080VS75000, Diodes:LED_0805_GREEN, F.Cu at (96.7, 89.4)
- added D202: 150080VS75000, Diodes:LED_0805_GREEN, F.Cu at (96.7, 85.9)
- added D203: 150080VS75000, Diodes:LED_0805_GREEN, F.Cu at (137.3, 77.6)
- added D204: 150080VS75000, Diodes:LED_0805_GREEN, F.Cu at (137.3, 81.1)
- added D205: 150080VS75000, Diodes:LED_0805_GREEN, F.Cu at (137.3, 84.6)
- added D301: 150080VS75000, Diodes:LED_0805_GREEN, F.Cu at (149.6, 137.0)
- added D302: 150080YS75000, Diodes:LED_0805_YELLOW, F.Cu at (149.6, 140.6)
- added D303: 150080RS75000, Diodes:LED_0805_RED, F.Cu at (149.6, 144.2)
- added D801: DSS16U, Diodes:SOD-123FL, F.Cu at (107.1, 131.8)
- added D802: DSS16U, Diodes:SOD-123FL, F.Cu at (107.1, 146.0)
- added F201: 39511000440, Fuses:TE5_395, F.Cu at (111.0, 97.9)
- added F202: 39511000440, Fuses:TE5_395, F.Cu at (151.4, 50.9)
- added F401: 0698Q6300-01, Fuses:TE5_395, F.Cu at (128.0, 47.8)
- added H101: Mounting-Hole-M3, Connectors:Mounting_Hole_3mm, F.Cu at (164.4, 188.9)
- added H102: Mounting-Hole-M3, Connectors:Mounting_Hole_3mm, F.Cu at (164.4, 38.9)
- added H103: Mounting-Hole-M3, Connectors:Mounting_Hole_3mm, F.Cu at (74.5, 38.9)
- added H104: Mounting-Hole-M3, Connectors:Mounting_Hole_3mm, F.Cu at (74.5, 188.9)
- added IC201: 1769205241, IC:1769205241, F.Cu at (128.7, 84.8)
- added J101: 2350514-8, Connectors:CONN8_2350514-8_TEC, F.Cu at (159.2, 149.0)
- added J201: Header_Male_Pin_2.54mm_1X2_,_Unshrouded, Connectors:Headers_2.54mm_1X2, F.Cu at (120.2, 128.1)
- added J202: 1935161, Connectors:1935161, F.Cu at (163.3, 53.3)
- added J203: 2350514-8, Connectors:CONN8_2350514-8_TEC, F.Cu at (79.3, 74.8)
- added J401: 1935161, Connectors:1935161, F.Cu at (140.2, 38.4)
- added J402: 1935161, Connectors:1935161, F.Cu at (128.0, 38.4)
- added J403: RF1-01K-D-00-50-BK-HDW, Connectors:RF101KD0050, F.Cu at (93.4, 46.7)
- added J404: RF1-01K-D-00-50-BK-HDW, Connectors:RF101KD0050, F.Cu at (111.2, 46.7)
- added J501: 2350514-8, Connectors:CONN8_2350514-8_TEC, F.Cu at (79.2, 106.4)
- added J502: XH-4A connector, Connectors:XH-4A, F.Cu at (152.6, 116.5)
- added J503: XH-4A connector, Connectors:XH-4A, F.Cu at (152.7, 106.9)
- added J504: 2350514-8, Connectors:CONN8_2350514-8_TEC, F.Cu at (159.2, 117.9)
- added J505: 2350514-8, Connectors:CONN8_2350514-8_TEC, F.Cu at (159.2, 88.2)
- added J601: 2350514-8, Connectors:CONN8_2350514-8_TEC, F.Cu at (159.2, 180.1)
- added J701: MEM2075-00-140-01-A, Connectors:GCT_MEM2075-00-140-01-A, F.Cu at (103.8, 185.3)
- added J801: 2350514-4, Connectors:CONN4_1155650000_TEC, F.Cu at (79.3, 138.1)
- added J802: 2350514-8, Connectors:CONN8_2350514-8_TEC, F.Cu at (79.2, 155.5)
- added Q401: MCB90N12A-TP, IC:MCB90N12ATP, F.Cu at (123.5, 60.6)
- added Q801: PMV20XNER, IC:SOT-23-3, F.Cu at (108.2, 138.9)
- added Q802: PMV20XNER, IC:SOT-23-3, F.Cu at (108.2, 153.2)
- added Q803: PMV20XNER, IC:SOT-23-3, F.Cu at (83.9, 159.0)
- added Q804: PMV20XNER, IC:SOT-23-3, F.Cu at (84.0, 166.0)
- added Q805: PMV20XNER, IC:SOT-23-3, F.Cu at (84.0, 172.9)
- added Q806: PMV20XNER, IC:SOT-23-3, F.Cu at (84.0, 180.0)
- added R201: RC0805FR-075K6L, Resistors:R0805, F.Cu at (101.1, 89.5)
- added R202: RC0805JR-072K2L, Resistors:R0805, F.Cu at (101.2, 85.9)
- added R203: RC0805JR-0733KL, Resistors:R0805, F.Cu at (141.6, 77.6)
- added R204: RC0805FR-075K6L, Resistors:R0805, F.Cu at (141.6, 81.1)
- added R205: RC0805JR-072K2L, Resistors:R0805, F.Cu at (141.6, 84.6)
- added R301: RC0805JR-074K7L, Resistors:R0805, F.Cu at (152.4, 152.5)
- added R302: RC0805JR-07150RL, Resistors:R0805, F.Cu at (149.6, 150.5)
- added R303: RC0805JR-072K2L, Resistors:R0805, F.Cu at (145.3, 136.9)
- added R304: RC0805JR-072K2L, Resistors:R0805, F.Cu at (145.3, 140.6)
- added R305: RC0805JR-072K2L, Resistors:R0805, F.Cu at (145.3, 144.2)
- added R401: RC0805JR-0710KL, Resistors:R0805, F.Cu at (112.6, -13.9)
- added R402: RC0805JR-07330RL, Resistors:R0805, F.Cu at (112.6, -10.4)
- added R403: RC0805JR-072K2L, Resistors:R0805, F.Cu at (112.6, -6.89)
- added R404: RC0805FR-075K6L, Resistors:R0805, F.Cu at (117.1, -13.9)
- added R405: ERJ-6ENF1404V, Resistors:R0805, F.Cu at (117.1, -10.4)
- added R406: RC0805JR-0710KL, Resistors:R0805, F.Cu at (117.1, -6.89)
- added R407: RC0805JR-0710KL, Resistors:R0805, F.Cu at (121.5, -13.9)
- added R408: RC0805FR-0747KL, Resistors:R0805, F.Cu at (121.5, -10.4)
- added R409: RC0805JR-0710KL, Resistors:R0805, F.Cu at (121.5, -6.89)
- added R410: ERJ-6ENF1404V, Resistors:R0805, F.Cu at (126.0, -13.9)
- added R411: RC0805JR-0710KL, Resistors:R0805, F.Cu at (126.0, -10.4)
- added R412: RC0805FR-0747KL, Resistors:R0805, F.Cu at (126.0, -6.89)
- added R501: RC0805JR-074K7L, Resistors:R0805, F.Cu at (136.4, 118.0)
- added R502: RC0805JR-074K7L, Resistors:R0805, F.Cu at (138.3, 118.0)
- added R503: RC0805JR-074K7L, Resistors:R0805, F.Cu at (136.4, 129.3)
- added R504: RC0805JR-074K7L, Resistors:R0805, F.Cu at (138.3, 129.3)
- added R505: RC0805JR-072K2L, Resistors:R0805, F.Cu at (103.8, 109.8)
- added R506: 0hms_0.5W, Resistors:R0805, F.Cu at (146.2, 93.3)
- added R507: RC0805JR-0710KL, Resistors:R0805, F.Cu at (99.0, 113.8)
- added R508: RC0805JR-0710KL, Resistors:R0805, F.Cu at (99.0, 109.8)
- added R509: 0hms_0.5W, Resistors:R0805, F.Cu at (146.2, 97.2)
- added R510: RC0805JR-072K2L, Resistors:R0805, F.Cu at (99.0, 118.8)
- added R511: RC0805JR-0710KL, Resistors:R0805, F.Cu at (94.0, 118.8)
- added R512: RC0805JR-0710KL, Resistors:R0805, F.Cu at (96.5, 118.8)
- added R513: RC0805JR-0710KL, Resistors:R0805, F.Cu at (142.9, 121.2)
- added R701: RC0805FR-0747KL, Resistors:R0805, F.Cu at (100.8, 167.7)
- added R702: RC0805JR-07150RL, Resistors:R0805, F.Cu at (98.3, 169.7)
- added R801: RC0805JR-07330RL, Resistors:R0805, F.Cu at (113.4, 140.2)
- added R802: RC0805JR-07330RL, Resistors:R0805, F.Cu at (113.4, 154.5)
- added R803: RC0805JR-0710KL, Resistors:R0805, F.Cu at (111.3, 137.6)
- added R804: RC0805JR-0710KL, Resistors:R0805, F.Cu at (111.3, 151.9)
- added R805: RC0805JR-07330RL, Resistors:R0805, F.Cu at (90.0, 159.9)
- added R806: RC0805JR-07330RL, Resistors:R0805, F.Cu at (90.0, 167.0)
- added R807: RC0805JR-07330RL, Resistors:R0805, F.Cu at (89.9, 173.9)
- added R808: RC0805JR-07330RL, Resistors:R0805, F.Cu at (89.9, 180.9)
- added R809: RC0805JR-0710KL, Resistors:R0805, F.Cu at (87.9, 157.3)
- added R810: RC0805JR-0710KL, Resistors:R0805, F.Cu at (87.9, 164.4)
- added R811: RC0805JR-0710KL, Resistors:R0805, F.Cu at (87.8, 171.3)
- added R812: RC0805JR-0710KL, Resistors:R0805, F.Cu at (87.8, 178.3)
- added RL801: ALQ312, Relays:ALQ312, F.Cu at (94.0, 135.0)
- added RL802: ALQ312, Relays:ALQ312, F.Cu at (94.0, 149.2)
- added SW301: PTS645SM43SMTR92, Switches:PTS645_6X6X4_SMD, F.Cu at (149.6, 157.6)
- added U201: AZ1117IH-3.3TRG1, IC:SOT-223-3, F.Cu at (111.5, 91.2)
- added U202: OKI-78SR-5_1.5-W36H-C, Assembly:OKI-78SR_Horizontal, F.Cu at (150.2, 59.0)
- added U203: AZ1117IH-3.3TRG1, IC:SOT-223-3, F.Cu at (127.0, 124.3)
- added U301: ESP32-DEVKITC-32D, Assembly:MODULE_ESP32-DEVKITC-32D, F.Cu at (129.3, 159.3)
- added U401: LTV-816S, IC:4-SMD, F.Cu at (127.8, 73.2)
- added U402: ADC124S021CIMM, IC:SOP50P490X110-10N, F.Cu at (112.1, 75.8)
- added U403: TMCS1101A3UQDT, IC:SOIC-8, F.Cu at (95.7, 66.6)
- added U404: ISO7341CQDWQ1, IC:SOIC-16-wide, F.Cu at (125.2, 100.1)
- added U405: MCP6L04T-E/SL, IC:SOIC127P600X175-14N, F.Cu at (99.6, -7.64)
- added U501: MCP4728T-E_UN, IC:SOP50P490X110-10N, F.Cu at (86.8, 111.9)
- added U502: TLV9302IDR, Assembly:IC8_TLV9302IDR_TEX, F.Cu at (94.0, 110.7)
- added U503: TLA2528IRTER, IC:QFN50P300X300X80-17N-D, F.Cu at (151.3, 96.7)
- added U504: TCA9617BDGKR, IC:SOP65P490X110-8N, F.Cu at (137.3, 123.4)
- added U601: 74LVC4245APW_118, IC:SOP65P640X110-24N, F.Cu at (150.6, 172.7)
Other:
- board size 100 x 100 mm -> 100 x 160 mm
- board text added: "3.3V (A)"
- board text added: "5V (A)"
- board text added: "DEBUG"
- board text added: "ERROR"
- board text added: "STATUS"
- board text added: "USER"
